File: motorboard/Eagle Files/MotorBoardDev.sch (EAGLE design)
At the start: 62 parts, among them J1 Under Glow, J2 B2PS-VH(LF)(SN), J3 B2PS-VH(LF)(SN), J4 B2PS-VH(LF)(SN), J5 B2PS-VH(LF)(SN), Q4 STT4P3LLH6, Q5 RRH100P03GZETB, T1 R-78E5.0-1.0, U1 9DoF IMU, U2 TXB0104DR, U4 TLV70233DBVR, U5 TC4427ACOA713, U6 TC4427ACOA713, U7 TC4427ACOA713, X1 MINI-USB_SHIELD5P4-32005-400, X2 C-GRID-05-15-91, X3 2510-, X4 2510-, X5 C-GRID-05-15-91, X6 C-GRID-02-70553, X7 SI-50170

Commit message: Finalized and should be ready to order
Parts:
- added J6: B2PS-VH(LF)(SN), RoboJackets-Connectors:B2PS-VH(LF)(SN)
- U2: value TXB0104DR -> TXB0106PWR; device MotorBoardDev:TXB0104DR -> MotorBoardDev:TXB0106PWR
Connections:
- new net MOTOR_CTRL: J6.2, U2.B1
- new net MOTOR_CTRL_3V3: A1.P$13, U2.A1
- net BLUE_3V3: now also A1.P$16; no longer A1.P$15
- net FRONT_LIGHT_3V3: now also A1.P$17; no longer A1.P$16
- net GND: now also J6.1
- net GREEN_3V3: now also A1.P$15; no longer A1.P$14
- net LEA: now also U2.B4; no longer U2.B3
- net LEA3: now also U2.A4; no longer U2.A3
- net LEB: now also U2.B5; no longer U2.B4
- net LEB3: now also U2.A5; no longer U2.A4
- net REA: now also U2.B2; no longer U2.B1
- net REA3: now also U2.A2; no longer U2.A1
- net REB: now also U2.B3; no longer U2.B2
- net REB3: now also U2.A3; no longer U2.A2
- net RED_3V3: now also A1.P$14; no longer A1.P$13
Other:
- note added: "Sawtooth Motor Controller"
- note added: "add level shifter for motor control"

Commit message: mbed test code and eagle side-notes
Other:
- note added: "For future design, make sure the level shifters can shift fast enough"
- note added: "Such as for high speed serial comm"
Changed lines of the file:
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@@
 <?xml version="1.0" encoding="utf-8"?>
 <!DOCTYPE eagle SYSTEM "eagle.dtd">
-<eagle version="8.4.2">
+<eagle version="8.5.2">
 <drawing>
 <settings>
@@
 <text x="64.77" y="5.08" size="2.54" layer="103" font="vector">Sawtooth Motor Controller</text>
 <text x="64.77" y="20.32" size="1.27" layer="103">add level shifter for motor control</text>
+<text x="73.66" y="119.38" size="1.778" layer="97">For future design, make sure the level
+shifters can shift fast enough</text>
+<text x="73.66" y="116.84" size="1.778" layer="97">Such as for high speed serial comm</text>
 </plain>
 <instances>

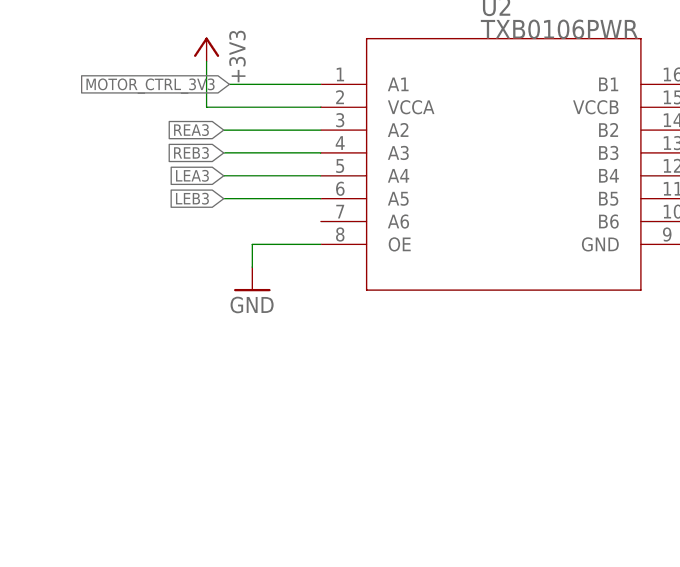
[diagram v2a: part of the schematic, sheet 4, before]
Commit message: Schematics update and Control code initial commit
Updated Motor board schematics with regard to the level shifter OE pin;
Initial commit to the migration of arduino code for motor shield to motor board.
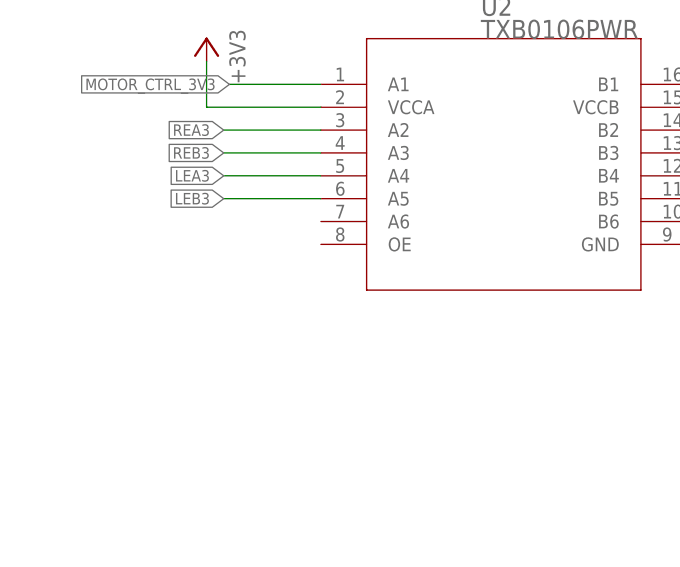
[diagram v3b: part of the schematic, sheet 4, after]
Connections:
- net GND: no longer U2.OE
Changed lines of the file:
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@@
 <?xml version="1.0" encoding="utf-8"?>
 <!DOCTYPE eagle SYSTEM "eagle.dtd">
-<eagle version="8.5.2">
+<eagle version="8.6.0">
 <drawing>
 <settings>
@@
 <part name="P+13" library="supply1" deviceset="+5V" device=""/>
 <part name="+3V37" library="supply1" deviceset="+3V3" device=""/>
-<part name="GND17" library="supply1" library_urn="urn:adsk.eagle:library:371" deviceset="GND" device=""/>
 <part name="GND19" library="supply1" library_urn="urn:adsk.eagle:library:371" deviceset="GND" device=""/>
 <part name="PS9" library="IGVC-Power" deviceset="LGND" device=""/>
@@
 <instance part="P+13" gate="1" x="99.06" y="106.68" rot="MR0"/>
 <instance part="+3V37" gate="G$1" x="30.48" y="106.68" rot="MR0"/>
-<instance part="GND17" gate="1" x="35.56" y="78.74"/>
 <instance part="GND19" gate="1" x="93.98" y="78.74"/>
 <instance part="R26" gate="G$1" x="139.7" y="185.42"/>
@@
 </segment>
 <segment>
-<pinref part="GND17" gate="1" pin="GND"/>
-<wire x1="35.56" y1="81.28" x2="35.56" y2="83.82" width="0.1524" layer="91"/>
-<wire x1="35.56" y1="83.82" x2="43.18" y2="83.82" width="0.1524" layer="91"/>
-<pinref part="U2" gate="A" pin="OE"/>
-</segment>
-<segment>
